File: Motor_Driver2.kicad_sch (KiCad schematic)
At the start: 20 parts, among them J701 Conn_01x02_Socket, U701 DMHT6016LFJ-13, U702 DRV8701

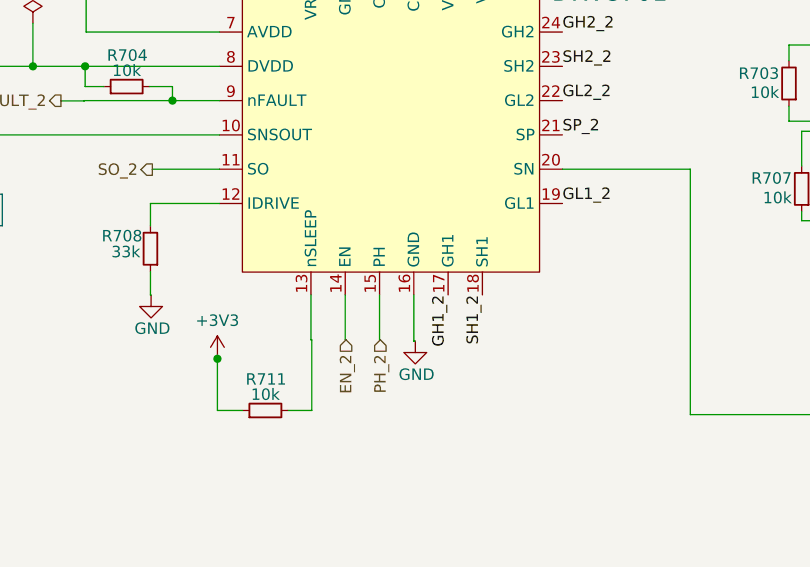
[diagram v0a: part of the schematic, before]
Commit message: critical nets coloured,some tracks rerouted, section 9 completed.
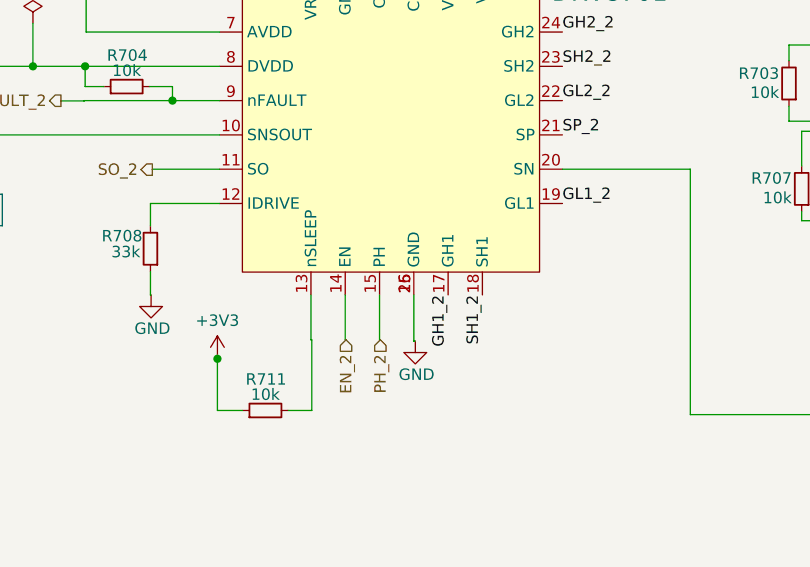
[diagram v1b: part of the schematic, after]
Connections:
- net GND: now also U702.25 (GND)
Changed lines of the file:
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@@
 		(pin "5"
+		)
+		(pin "25"
 		)
 		(instances

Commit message: schematic pages are reviewed
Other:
- note added: "H-BRIDGE"
- note added: "MOTOR DRIVER 2"
- moved on the sheet: J701
